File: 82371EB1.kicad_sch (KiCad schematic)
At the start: 3 parts, among them U23 82371EB

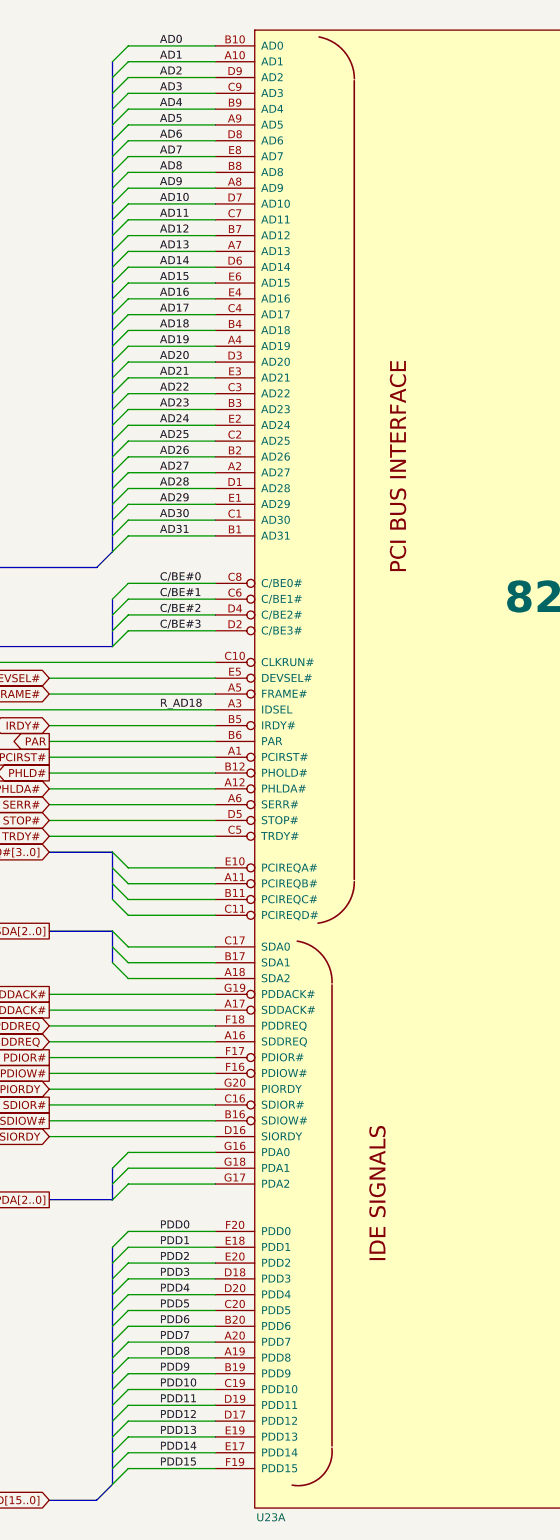
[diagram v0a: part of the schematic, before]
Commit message: page 6,7,8 82443BX chipset, various small fixes
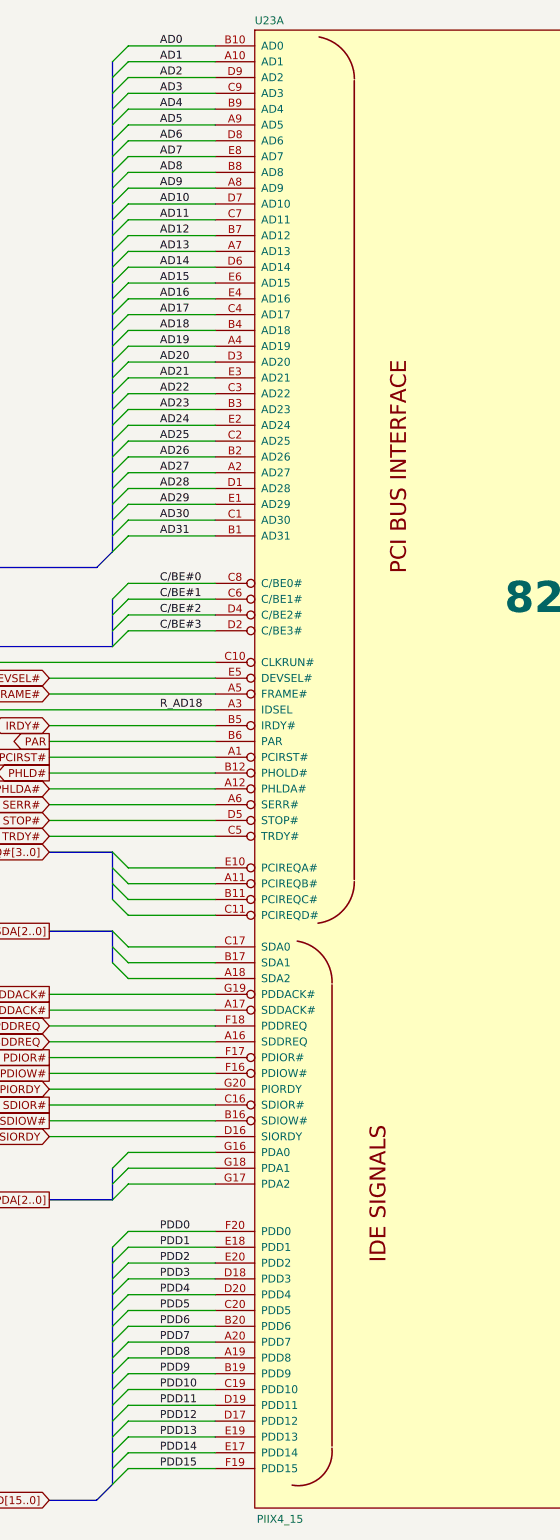
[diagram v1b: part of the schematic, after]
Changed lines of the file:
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@@
 		(dnp no)
 		(property "Reference" "U23"
-			(at 112.014 259.334 0)
+			(at 111.76 18.796 0)
 			(effects
 				(font
@@
 			)
 		)
-		(property "Datasheet" "blah"
+		(property "Datasheet" ""
 			(at -6.604 -242.57 0)
 			(effects
@@
 			)
 		)
-		(property "Description" "BXChipset"
-			(at -6.604 -252.73 0)
+		(property "Description" "PIIX4_15"
+			(at 115.824 259.588 0)
 			(effects
 				(font
 					(size 1.27 1.27)
 				)
-				(hide yes)
 			)
 		)
